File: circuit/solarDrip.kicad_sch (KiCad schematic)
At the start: 41 parts, among them J1 solar_charger, J2 batt, J3 solar, J4 pump, J5 soil, J6 water, J7 USB_C_Receptacle_USB2.0_14P, J8 i2c, Q1 2N7002K, Q2 2N7002K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

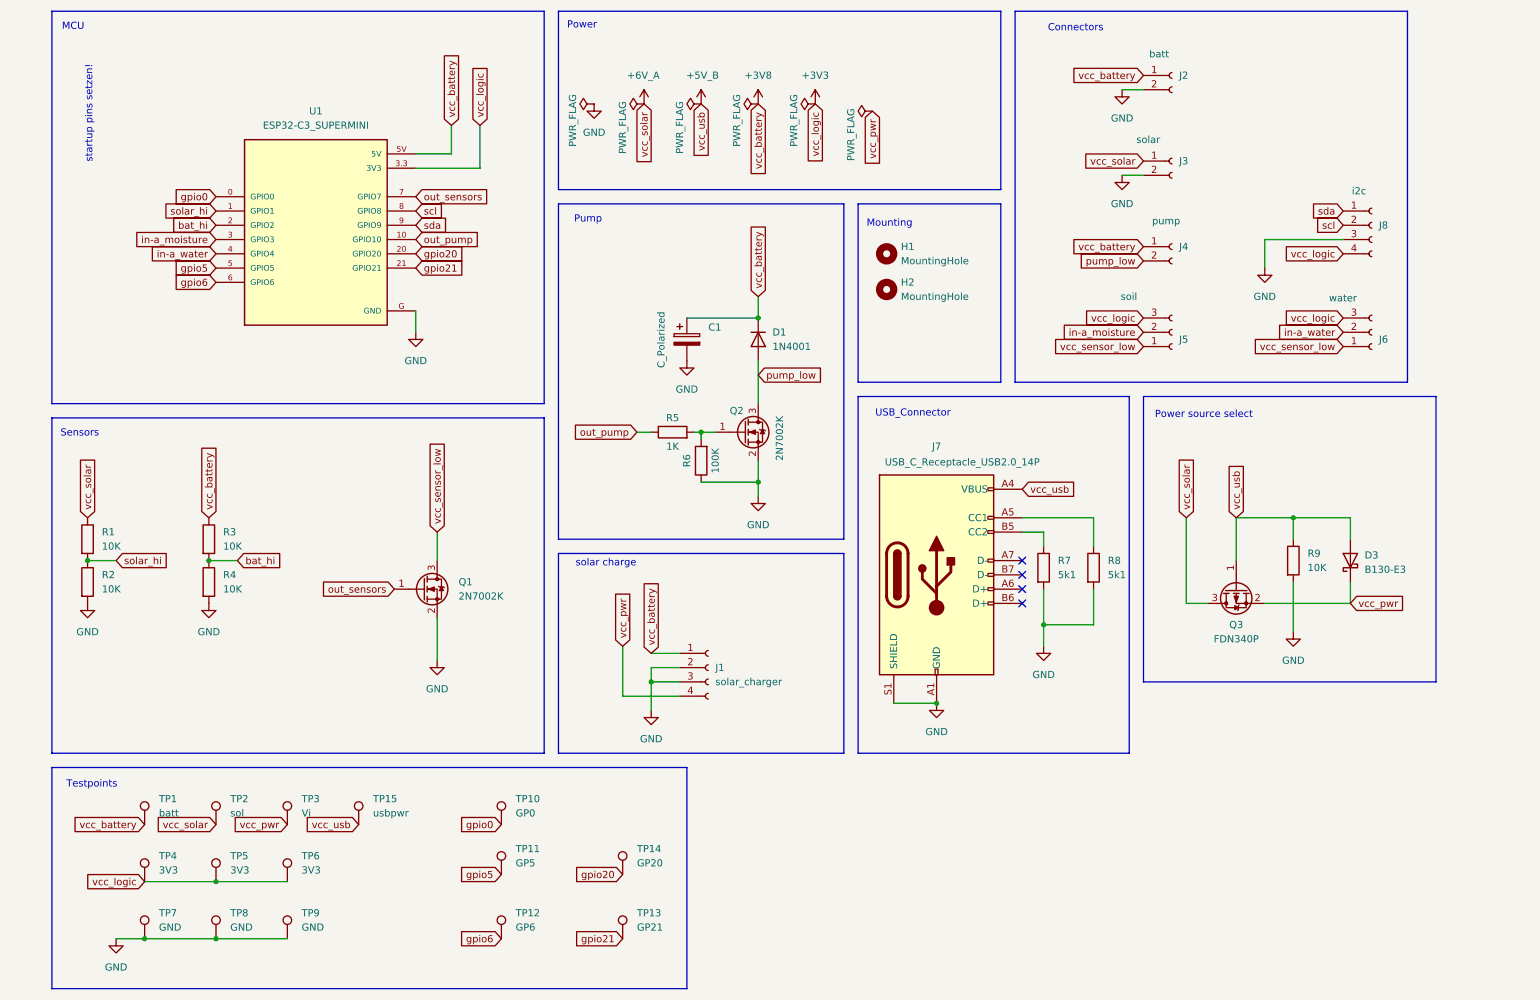
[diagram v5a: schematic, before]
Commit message: add motor cap
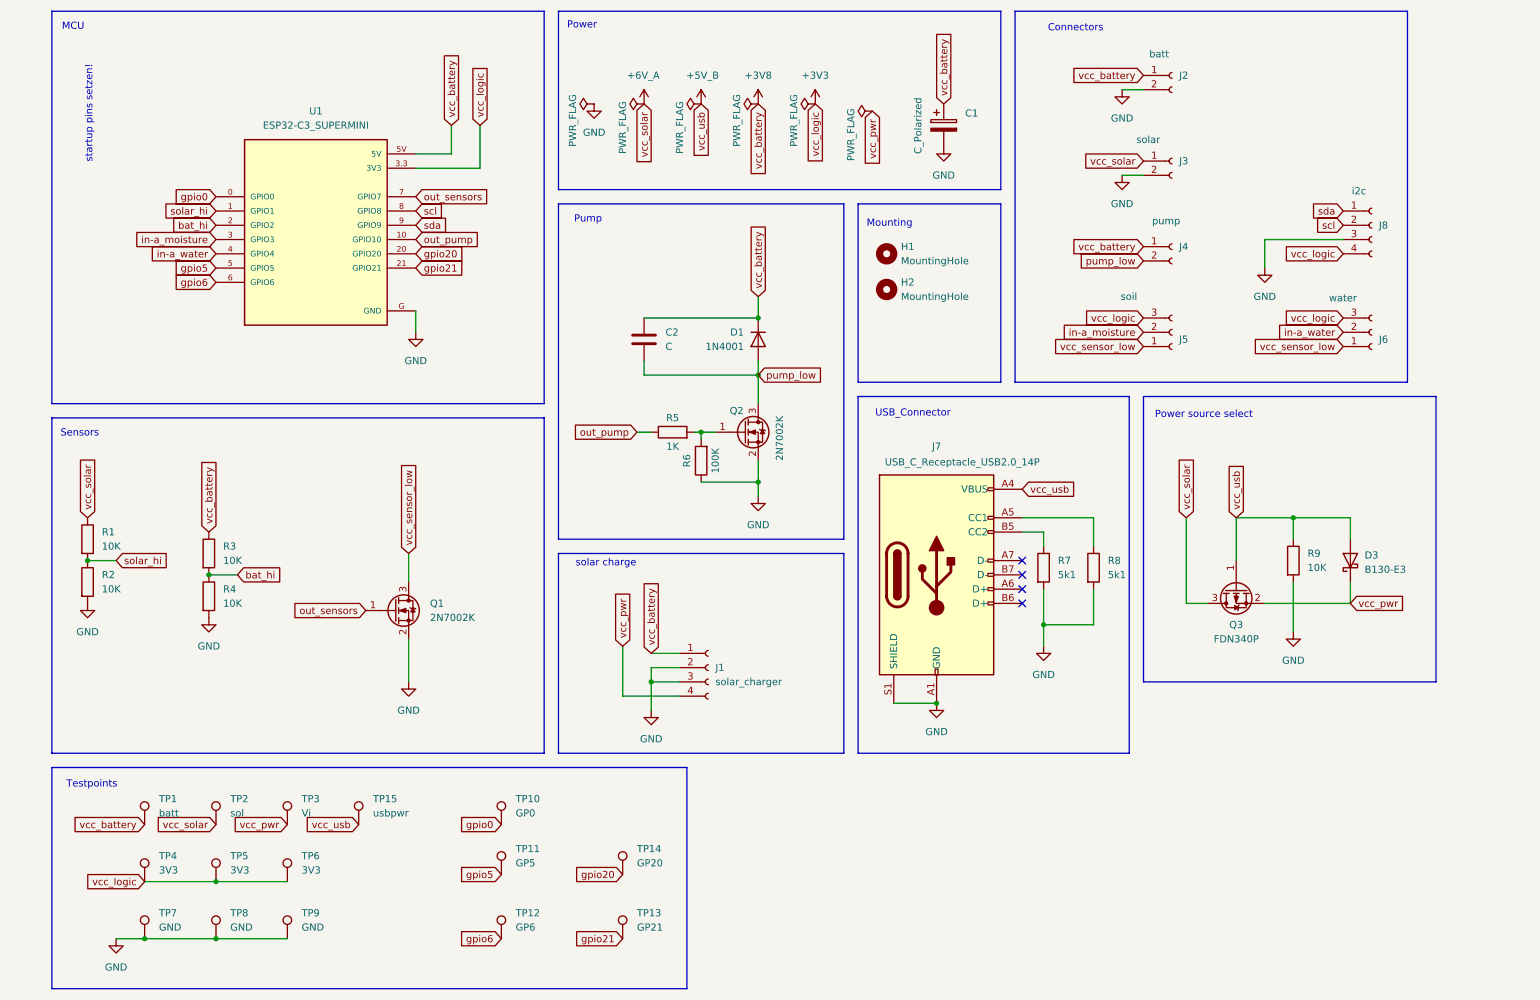
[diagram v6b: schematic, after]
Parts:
- added C2: C, Capacitor_SMD:C_1206_3216Metric_Pad1.33x1.80mm_HandSolder, symbol Device:C
- C1: footprint Capacitor_THT:CP_Radial_D10.0mm_P7.50mm -> Capacitor_THT:CP_Radial_D8.0mm_P3.80mm
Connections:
- net +3V8: now also C2.1
- net pump_low: now also C2.2
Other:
- moved on the sheet: C1, D1, Q1, R3, R4

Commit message: add additional pads for smd/tht sockets
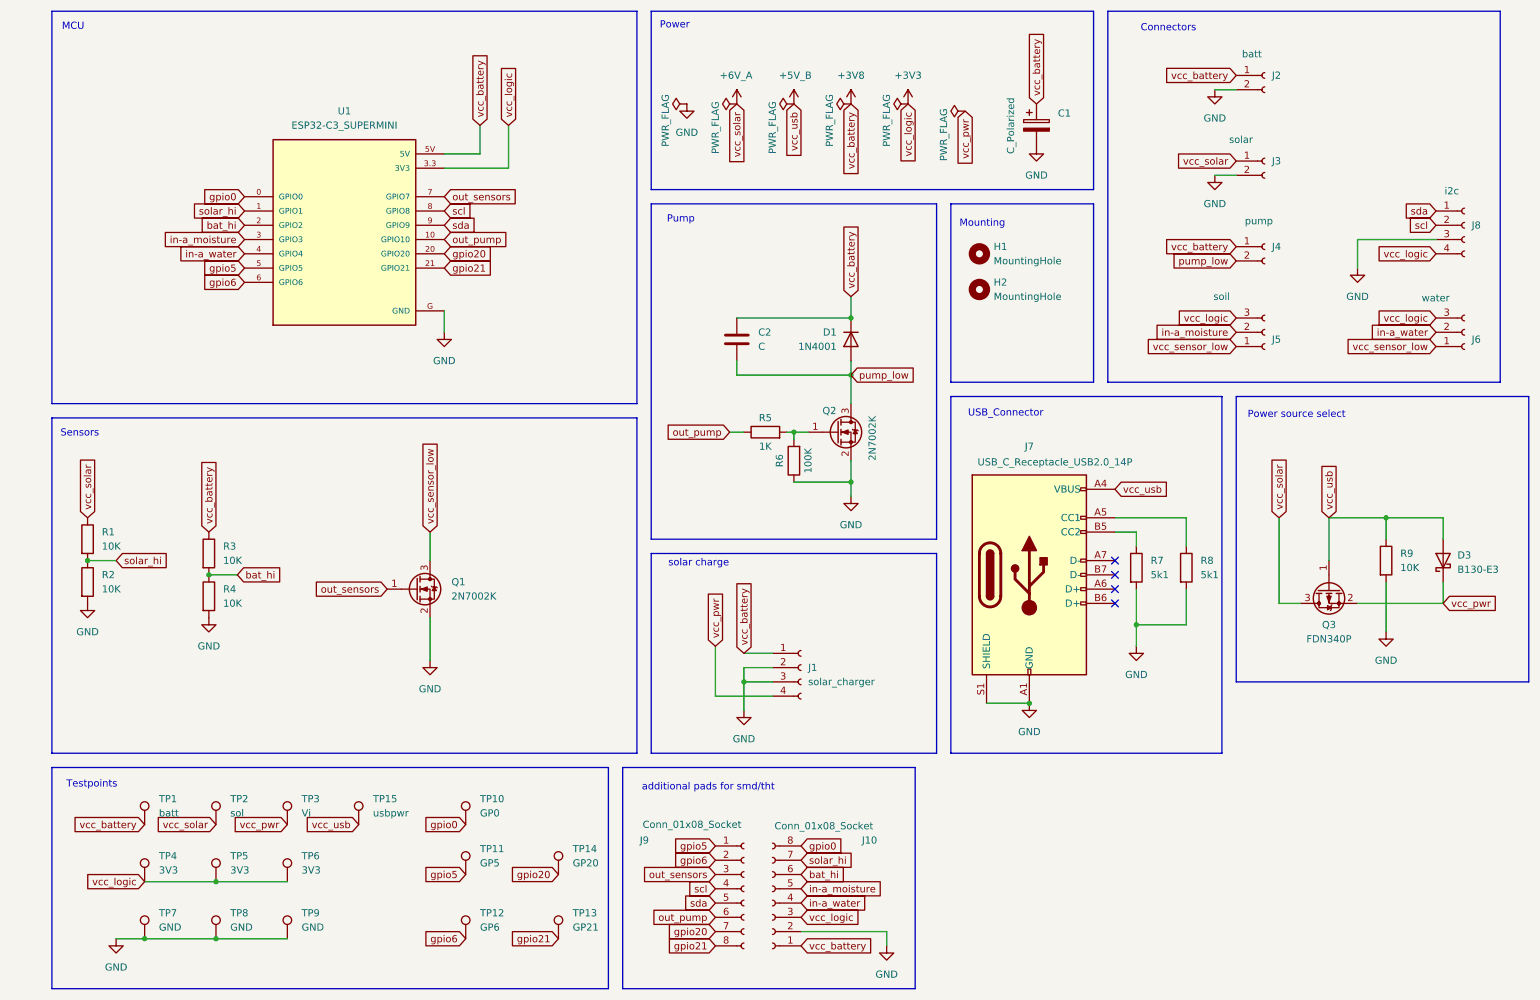
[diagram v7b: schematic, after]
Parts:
- added J10, J9: Conn_01x08_Socket, symbol Connector:Conn_01x08_Socket
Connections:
- net +3V3: now also J10.3 (Pin_3)
- net +3V8: now also J10.1 (Pin_1)
- net GND: now also J10.2 (Pin_2)
- net bat_hi: now also J10.6 (Pin_6)
- net gpio0: now also J10.8 (Pin_8)
- net gpio20: now also J9.7 (Pin_7)
- net gpio21: now also J9.8 (Pin_8)
- net gpio5: now also J9.1 (Pin_1)
- net gpio6: now also J9.2 (Pin_2)
- net in-a_moisture: now also J10.5 (Pin_5)
- net in-a_water: now also J10.4 (Pin_4)
- net out_pump: now also J9.6 (Pin_6)
- net out_sensors: now also J9.3 (Pin_3)
- net scl: now also J9.4 (Pin_4)
- net sda: now also J9.5 (Pin_5)
- net solar_hi: now also J10.7 (Pin_7)
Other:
- note added: "additional pads for smd/tht"
- note removed: "startup pins setzen!"
- moved on the sheet: C1, C2, D1, D3, H1, H2, J1, J2, J3, J4, J5, J6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

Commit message: pcb: add U1 smd pads
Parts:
- J10, J9: footprint (none) -> Connector_PinSocket_2.54mm:PinSocket_1x08_P2.54mm_Vertical_SMD_Pin1Left
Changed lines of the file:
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@@
 			)
 		)
-		(property "Footprint" ""
+		(property "Footprint" "Connector_PinSocket_2.54mm:PinSocket_1x08_P2.54mm_Vertical_SMD_Pin1Left"
 			(at 143.51 172.72 0)
 			(effects
@@
 			)
 		)
-		(property "Footprint" ""
+		(property "Footprint" "Connector_PinSocket_2.54mm:PinSocket_1x08_P2.54mm_Vertical_SMD_Pin1Left"
 			(at 148.59 175.26 0)
 			(effects
